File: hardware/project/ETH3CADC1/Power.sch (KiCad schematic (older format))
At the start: 6 parts, among them U1501 LM337_SOT223

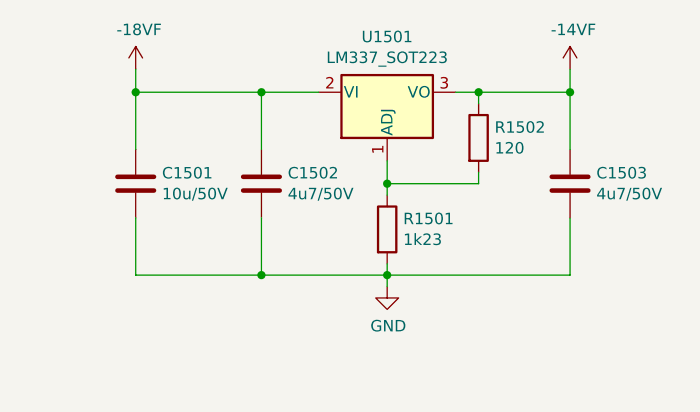
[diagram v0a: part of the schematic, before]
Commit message: SDRAM works, thanks to the website https://medium.com/@pjinwoo123/stm32h7-external-sdram-evaluation-board-cc72444898d8 . Modified the code to work with SDRAM BANK2. SCPI library works.
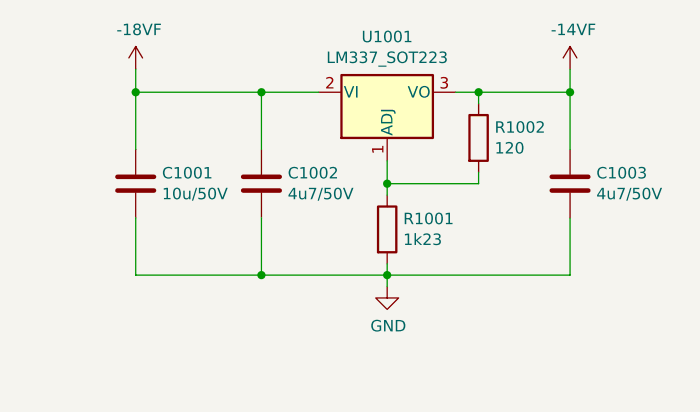
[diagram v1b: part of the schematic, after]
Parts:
- renumbered C1501 to C1001, C1502 to C1002, C1503 to C1003, R1501 to R1001, R1502 to R1002, U1501 to U1001
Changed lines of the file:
@@
 $Descr A4 11693 8268
 encoding utf-8
-Sheet 15 15
+Sheet 10 13
 Title ""
 Date ""
@@
 $EndDescr
 $Comp
-L Regulator_Linear:LM337_SOT223 U1501
+L Regulator_Linear:LM337_SOT223 U1001
 U 1 1 5FE71A52
 P 5100 3450
-F 0 "U1501" H 5100 3208 50  0000 C CNN
+F 0 "U1001" H 5100 3208 50  0000 C CNN
 F 1 "LM337_SOT223" H 5100 3299 50  0000 C CNN
 F 2 "Package_TO_SOT_SMD:SOT-223-3_TabPin2" H 5100 3250 50  0001 C CIN
@@
 $EndComp
 $Comp
-L ETH3CDAQ1:-18VF #PWR01503
+L ETH3CDAQ1:-18VF #PWR01003
 U 1 1 5FE71F83
 P 4000 3350
-F 0 "#PWR01503" H 4000 3200 50  0001 C CNN
+F 0 "#PWR01003" H 4000 3200 50  0001 C CNN
 F 1 "-18VF" H 4015 3523 50  0000 C CNN
 F 2 "" H 4000 3350 50  0001 C CNN
@@
 $EndComp
 $Comp
-L Device:C C1502
+L Device:C C1002
 U 1 1 5FE72614
 P 4550 3850
-F 0 "C1502" H 4665 3896 50  0000 L CNN
+F 0 "C1002" H 4665 3896 50  0000 L CNN
 F 1 "4u7/50V" H 4665 3805 50  0000 L CNN
 F 2 "Capacitor_SMD:C_0805_2012Metric_Pad1.18x1.45mm_HandSolder" H 4588 3700 50  0001 C CNN
@@
 $EndComp
 $Comp
-L Device:C C1501
+L Device:C C1001
 U 1 1 5FE72AD1
 P 4000 3850
-F 0 "C1501" H 4115 3896 50  0000 L CNN
+F 0 "C1001" H 4115 3896 50  0000 L CNN
 F 1 "10u/50V" H 4115 3805 50  0000 L CNN
 F 2 "Capacitor_SMD:C_0805_2012Metric_Pad1.18x1.45mm_HandSolder" H 4038 3700 50  0001 C CNN
@@
 	4550 3450 4000 3450
 $Comp
-L Device:R R1502
+L Device:R R1002
 U 1 1 5FE76A3B
 P 5500 3650
-F 0 "R1502" H 5570 3696 50  0000 L CNN
+F 0 "R1002" H 5570 3696 50  0000 L CNN
 F 1 "120" H 5570 3605 50  0000 L CNN
 F 2 "Resistor_SMD:R_0402_1005Metric_Pad0.72x0.64mm_HandSolder" V 5430 3650 50  0001 C CNN
@@
 $EndComp
 $Comp
-L Device:R R1501
+L Device:R R1001
 U 1 1 5FE76E97
 P 5100 4050
-F 0 "R1501" H 5170 4096 50  0000 L CNN
+F 0 "R1001" H 5170 4096 50  0000 L CNN
 F 1 "1k23" H 5170 4005 50  0000 L CNN
 F 2 "Resistor_SMD:R_0402_1005Metric_Pad0.72x0.64mm_HandSolder" V 5030 4050 50  0001 C CNN
@@
 	4550 4250 5100 4250
 $Comp
-L power:GND #PWR01504
+L power:GND #PWR01004
 U 1 1 5FE7B8AD
 P 5100 4300
-F 0 "#PWR01504" H 5100 4050 50  0001 C CNN
+F 0 "#PWR01004" H 5100 4050 50  0001 C CNN
 F 1 "GND" H 5105 4127 50  0000 C CNN
 F 2 "" H 5100 4300 50  0001 C CNN
@@
 Connection ~ 5100 4250
 $Comp
-L ETH3CDAQ1:AGNDF #PWR01501
+L ETH3CDAQ1:AGNDF #PWR01001
 U 1 1 5FE7C633
 P 1500 6600
-F 0 "#PWR01501" H 1500 6350 50  0001 C CNN
+F 0 "#PWR01001" H 1500 6350 50  0001 C CNN
 F 1 "AGNDF" H 1505 6427 50  0000 C CNN
 F 2 "" H 1500 6600 50  0001 C CNN
@@
 $EndComp
 $Comp
-L power:GND #PWR01502
+L power:GND #PWR01002
 U 1 1 5FE7CB37
 P 1850 6600
-F 0 "#PWR01502" H 1850 6350 50  0001 C CNN
+F 0 "#PWR01002" H 1850 6350 50  0001 C CNN
 F 1 "GND" H 1855 6427 50  0000 C CNN
 F 2 "" H 1850 6600 50  0001 C CNN
@@
 	1500 6550 1500 6600
 $Comp
-L Device:C C1503
+L Device:C C1003
 U 1 1 5FE80B87
 P 5900 3850
-F 0 "C1503" H 6015 3896 50  0000 L CNN
+F 0 "C1003" H 6015 3896 50  0000 L CNN
 F 1 "4u7/50V" H 6015 3805 50  0000 L CNN
 F 2 "Capacitor_SMD:C_0805_2012Metric_Pad1.18x1.45mm_HandSolder" H 5938 3700 50  0001 C CNN
@@
 	5900 4250 5900 4000
 $Comp
-L ETH3CDAQ1:-14VF #PWR01505
+L ETH3CDAQ1:-14VF #PWR01005
 U 1 1 5FE836DD
 P 5900 3350
-F 0 "#PWR01505" H 5900 3200 50  0001 C CNN
+F 0 "#PWR01005" H 5900 3200 50  0001 C CNN
 F 1 "-14VF" H 5915 3523 50  0000 C CNN
 F 2 "" H 5900 3350 50  0001 C CNN

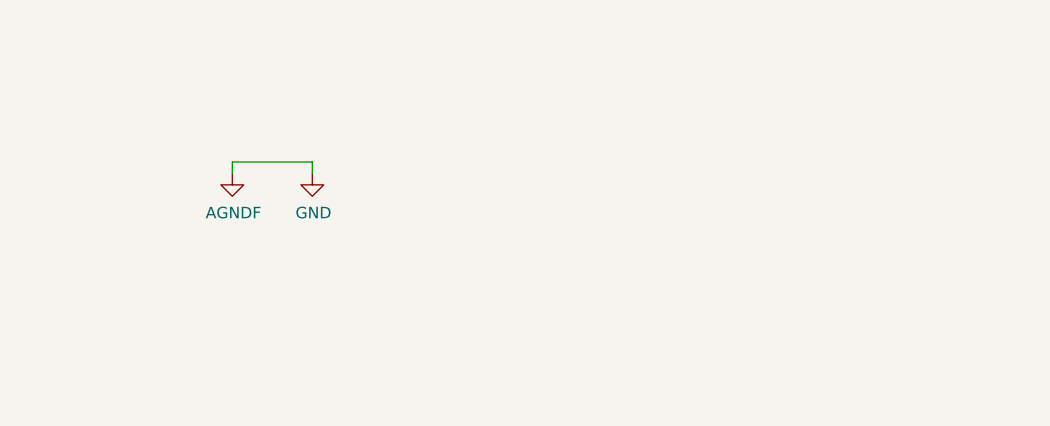
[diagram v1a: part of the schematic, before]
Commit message: Added SDRAM to the linker file.
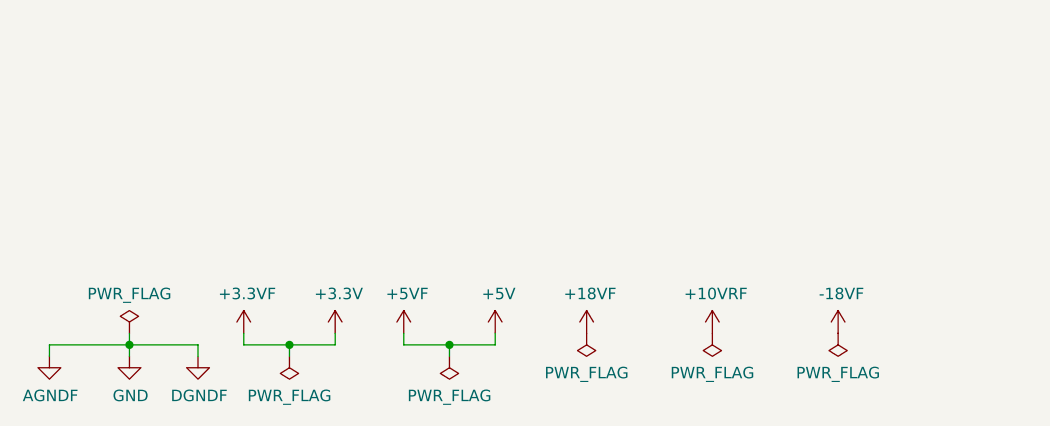
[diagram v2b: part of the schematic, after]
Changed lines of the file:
@@
 $EndComp
 $Comp
-L ETH3CDAQ1:-18VF #PWR01003
+L ETH3CDAQ1:-18VF #PWR01010
 U 1 1 5FE71F83
 P 4000 3350
-F 0 "#PWR01003" H 4000 3200 50  0001 C CNN
+F 0 "#PWR01010" H 4000 3200 50  0001 C CNN
 F 1 "-18VF" H 4015 3523 50  0000 C CNN
 F 2 "" H 4000 3350 50  0001 C CNN
@@
 	4550 4250 5100 4250
 $Comp
-L power:GND #PWR01004
+L power:GND #PWR01012
 U 1 1 5FE7B8AD
 P 5100 4300
-F 0 "#PWR01004" H 5100 4050 50  0001 C CNN
+F 0 "#PWR01012" H 5100 4050 50  0001 C CNN
 F 1 "GND" H 5105 4127 50  0000 C CNN
 F 2 "" H 5100 4300 50  0001 C CNN
@@
 L ETH3CDAQ1:AGNDF #PWR01001
 U 1 1 5FE7C633
-P 1500 6600
-F 0 "#PWR01001" H 1500 6350 50  0001 C CNN
-F 1 "AGNDF" H 1505 6427 50  0000 C CNN
-F 2 "" H 1500 6600 50  0001 C CNN
-F 3 "" H 1500 6600 50  0001 C CNN
-	1    1500 6600
+P 700 7400
+F 0 "#PWR01001" H 700 7150 50  0001 C CNN
+F 1 "AGNDF" H 705 7227 50  0000 C CNN
+F 2 "" H 700 7400 50  0001 C CNN
+F 3 "" H 700 7400 50  0001 C CNN
+	1    700  7400
 	1    0    0    -1
 $EndComp
@@
 L power:GND #PWR01002
 U 1 1 5FE7CB37
-P 1850 6600
-F 0 "#PWR01002" H 1850 6350 50  0001 C CNN
-F 1 "GND" H 1855 6427 50  0000 C CNN
-F 2 "" H 1850 6600 50  0001 C CNN
-F 3 "" H 1850 6600 50  0001 C CNN
-	1    1850 6600
-	1    0    0    -1
-$EndComp
-Wire Wire Line
-	1850 6600 1850 6550
-Wire Wire Line
-	1850 6550 1500 6550
-Wire Wire Line
-	1500 6550 1500 6600
+P 1050 7400
+F 0 "#PWR01002" H 1050 7150 50  0001 C CNN
+F 1 "GND" H 1055 7227 50  0000 C CNN
+F 2 "" H 1050 7400 50  0001 C CNN
+F 3 "" H 1050 7400 50  0001 C CNN
+	1    1050 7400
+	1    0    0    -1
+$EndComp
+Wire Wire Line
+	1050 7400 1050 7350
+Wire Wire Line
+	1050 7350 700  7350
+Wire Wire Line
+	700  7350 700  7400
 $Comp
 L Device:C C1003
@@
 	5900 4250 5900 4000
 $Comp
-L ETH3CDAQ1:-14VF #PWR01005
+L ETH3CDAQ1:-14VF #PWR01013
 U 1 1 5FE836DD
 P 5900 3350
-F 0 "#PWR01005" H 5900 3200 50  0001 C CNN
+F 0 "#PWR01013" H 5900 3200 50  0001 C CNN
 F 1 "-14VF" H 5915 3523 50  0000 C CNN
 F 2 "" H 5900 3350 50  0001 C CNN
@@
 	5900 3350 5900 3450
 Connection ~ 5900 3450
+$Comp
+L ETH3CDAQ1:+3.3VF #PWR01004
+U 1 1 602E7044
+P 1550 7300
+F 0 "#PWR01004" H 1550 7150 50  0001 C CNN
+F 1 "+3.3VF" H 1565 7473 50  0000 C CNN
+F 2 "" H 1550 7300 50  0001 C CNN
+F 3 "" H 1550 7300 50  0001 C CNN
+	1    1550 7300
+	1    0    0    -1
+$EndComp
+$Comp
+L power:+3.3V #PWR01005
+U 1 1 602E79D4
+P 1950 7300
+F 0 "#PWR01005" H 1950 7150 50  0001 C CNN
+F 1 "+3.3V" H 1965 7473 50  0000 C CNN
+F 2 "" H 1950 7300 50  0001 C CNN
+F 3 "" H 1950 7300 50  0001 C CNN
+	1    1950 7300
+	1    0    0    -1
+$EndComp
+Wire Wire Line
+	1550 7300 1550 7350
+Wire Wire Line
+	1550 7350 1750 7350
+Wire Wire Line
+	1950 7350 1950 7300
+$Comp
+L ETH3CDAQ1:+18VF #PWR01008
+U 1 1 602EF4E8
+P 3050 7300
+F 0 "#PWR01008" H 3050 7150 50  0001 C CNN
+F 1 "+18VF" H 3065 7473 50  0000 C CNN
+F 2 "" H 3050 7300 50  0001 C CNN
+F 3 "" H 3050 7300 50  0001 C CNN
+	1    3050 7300
+	1    0    0    -1
+$EndComp
+$Comp
+L power:PWR_FLAG #FLG01004
+U 1 1 602EFA20
+P 3050 7300
+F 0 "#FLG01004" H 3050 7375 50  0001 C CNN
+F 1 "PWR_FLAG" H 3050 7473 50  0000 C CNN
+F 2 "" H 3050 7300 50  0001 C CNN
+F 3 "~" H 3050 7300 50  0001 C CNN
+	1    3050 7300
+	-1   0    0    1
+$EndComp
+$Comp
+L ETH3CDAQ1:+10VRF #PWR01009
+U 1 1 602F7A2A
+P 3600 7300
+F 0 "#PWR01009" H 3600 7150 50  0001 C CNN
+F 1 "+10VRF" H 3615 7473 50  0000 C CNN
+F 2 "" H 3600 7300 50  0001 C CNN
+F 3 "" H 3600 7300 50  0001 C CNN
+	1    3600 7300
+	1    0    0    -1
+$EndComp
+$Comp
+L power:PWR_FLAG #FLG01005
+U 1 1 602F7F2A
+P 3600 7300
+F 0 "#FLG01005" H 3600 7375 50  0001 C CNN
+F 1 "PWR_FLAG" H 3600 7473 50  0000 C CNN
+F 2 "" H 3600 7300 50  0001 C CNN
+F 3 "~" H 3600 7300 50  0001 C CNN
+	1    3600 7300
+	-1   0    0    1
+$EndComp
+$Comp
+L ETH3CDAQ1:DGNDF #PWR01003
+U 1 1 60311DC4
+P 1350 7400
+F 0 "#PWR01003" H 1350 7150 50  0001 C CNN
+F 1 "DGNDF" H 1355 7227 50  0000 C CNN
+F 2 "" H 1350 7400 50  0001 C CNN
+F 3 "" H 1350 7400 50  0001 C CNN
+	1    1350 7400
+	1    0    0    -1
+$EndComp
+Wire Wire Line
+	1050 7350 1350 7350
+Wire Wire Line
+	1350 7350 1350 7400
+Connection ~ 1050 7350
+$Comp
+L power:PWR_FLAG #FLG01001
+U 1 1 60316FCD
+P 1050 7300
+F 0 "#FLG01001" H 1050 7375 50  0001 C CNN
+F 1 "PWR_FLAG" H 1050 7473 50  0000 C CNN
+F 2 "" H 1050 7300 50  0001 C CNN
+F 3 "~" H 1050 7300 50  0001 C CNN
+	1    1050 7300
+	1    0    0    -1
+$EndComp
+Wire Wire Line
+	1050 7300 1050 7350
+$Comp
+L power:PWR_FLAG #FLG01002
+U 1 1 60317C89
+P 1750 7400
+F 0 "#FLG01002" H 1750 7475 50  0001 C CNN
+F 1 "PWR_FLAG" H 1750 7573 50  0000 C CNN
+F 2 "" H 1750 7400 50  0001 C CNN
+F 3 "~" H 1750 7400 50  0001 C CNN
+	1    1750 7400
+	-1   0    0    1
+$EndComp
+Wire Wire Line
+	1750 7400 1750 7350
+Connection ~ 1750 7350
+Wire Wire Line
+	1750 7350 1950 7350
+$Comp
+L ETH3CDAQ1:+5VF #PWR01006
+U 1 1 60329460
+P 2250 7300
+F 0 "#PWR01006" H 2250 7150 50  0001 C CNN
+F 1 "+5VF" H 2265 7473 50  0000 C CNN
+F 2 "" H 2250 7300 50  0001 C CNN
+F 3 "" H 2250 7300 50  0001 C CNN
+	1    2250 7300
+	1    0    0    -1
+$EndComp
+Wire Wire Line
+	2250 7300 2250 7350
+Wire Wire Line
+	2250 7350 2450 7350
+Wire Wire Line
+	2650 7350 2650 7300
+$Comp
+L power:PWR_FLAG #FLG01003
+U 1 1 603EAC72
+P 2450 7400
+F 0 "#FLG01003" H 2450 7475 50  0001 C CNN
+F 1 "PWR_FLAG" H 2450 7573 50  0000 C CNN
+F 2 "" H 2450 7400 50  0001 C CNN
+F 3 "~" H 2450 7400 50  0001 C CNN
+	1    2450 7400
+	-1   0    0    1
+$EndComp
+Wire Wire Line
+	2450 7400 2450 7350
+Connection ~ 2450 7350
+Wire Wire Line
+	2450 7350 2650 7350
+$Comp
+L power:+5V #PWR01007
+U 1 1 603ED14D
+P 2650 7300
+F 0 "#PWR01007" H 2650 7150 50  0001 C CNN
+F 1 "+5V" H 2665 7473 50  0000 C CNN
+F 2 "" H 2650 7300 50  0001 C CNN
+F 3 "" H 2650 7300 50  0001 C CNN
+	1    2650 7300
+	1    0    0    -1
+$EndComp
+$Comp
+L power:PWR_FLAG #FLG01006
+U 1 1 603F6856
+P 4150 7300
+F 0 "#FLG01006" H 4150 7375 50  0001 C CNN
+F 1 "PWR_FLAG" H 4150 7473 50  0000 C CNN
+F 2 "" H 4150 7300 50  0001 C CNN
+F 3 "~" H 4150 7300 50  0001 C CNN
+	1    4150 7300
+	-1   0    0    1
+$EndComp
+$Comp
+L ETH3CDAQ1:-18VF #PWR01011
+U 1 1 603F785A
+P 4150 7300
+F 0 "#PWR01011" H 4150 7150 50  0001 C CNN
+F 1 "-18VF" H 4165 7473 50  0000 C CNN
+F 2 "" H 4150 7300 50  0001 C CNN
+F 3 "" H 4150 7300 50  0001 C CNN
+	1    4150 7300
+	1    0    0    -1
+$EndComp
 $EndSCHEMATC
